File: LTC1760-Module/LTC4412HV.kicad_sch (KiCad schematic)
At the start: 5 parts, among them Q3 Si7463DP, U9 LTC4412HVIS6

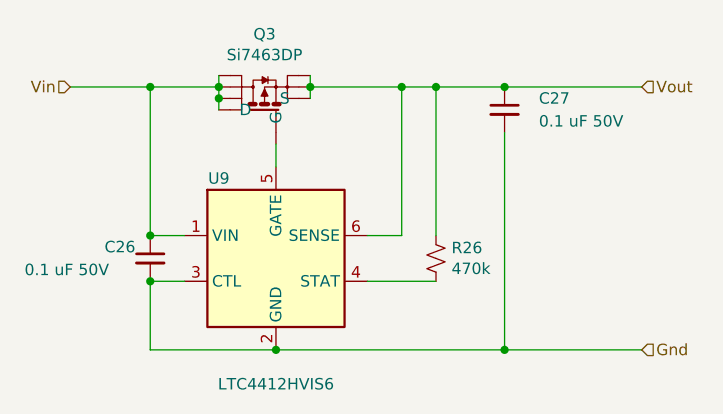
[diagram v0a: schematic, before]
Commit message: slight updates to LTC1670 modules (2 resistors added) finalizing console controller and strobe controller
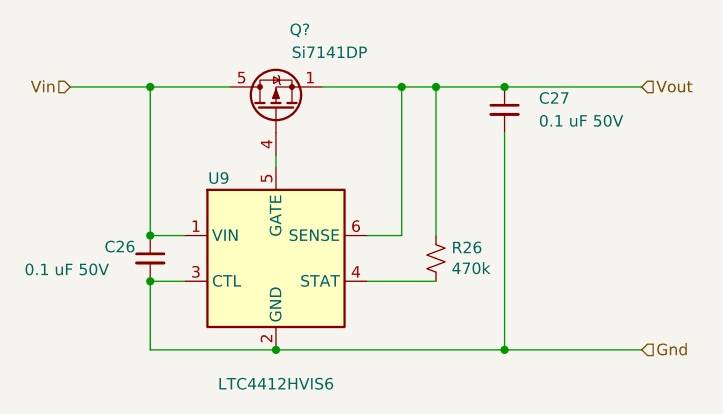
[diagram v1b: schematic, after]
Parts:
- removed Q3: Si7463DP, Package_SO:PowerPAK_SO-8_Single, symbol ProjectDevices:Si7463DP
- added Q?: Si7141DP, Package_SO:PowerPAK_SO-8_Single, symbol Transistor_FET:Si7141DP
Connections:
- net Vin: now also Q?.5 (D)
- net Vout: now also Q?.1 (S), Q?.2 (S), Q?.3 (S)
- net at U9.5 (GATE): now also Q?.4 (G)
